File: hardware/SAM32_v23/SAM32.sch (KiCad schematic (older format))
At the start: 54 parts, among them J1 10118194-0001LF, J2 Conn_01x14, J3 5031821852, J4 B2B-PH-SM4-TB, J5 NPTC072KFMS-RC, J7 Conn_01x17, J96 MOUNTINGHOLE2.5, J97 MOUNTINGHOLE2.5, Q3 DMG341, SW1 KMR231NG LFS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

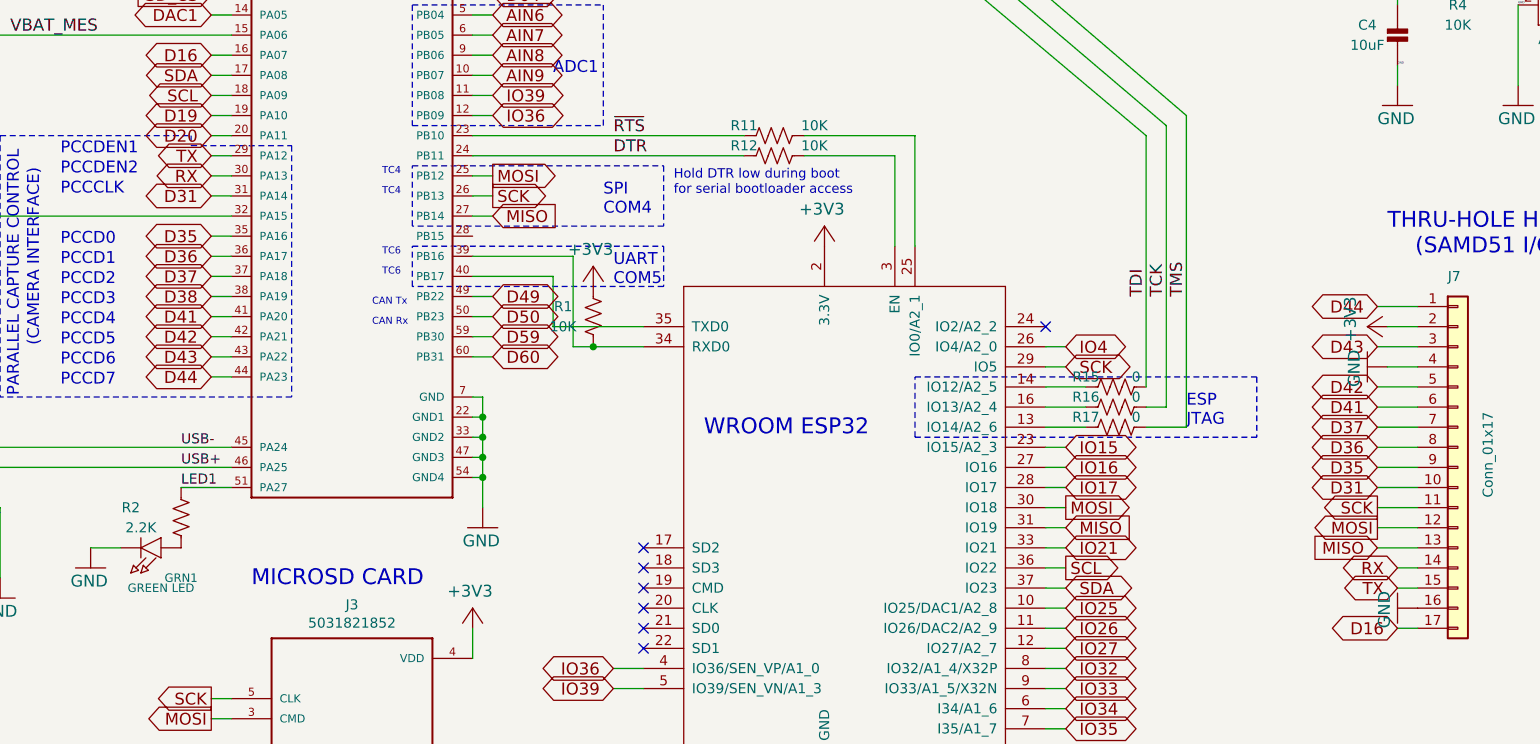
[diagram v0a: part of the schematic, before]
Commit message: adding esp32SPI firmware and clarification edits on v23 schematic
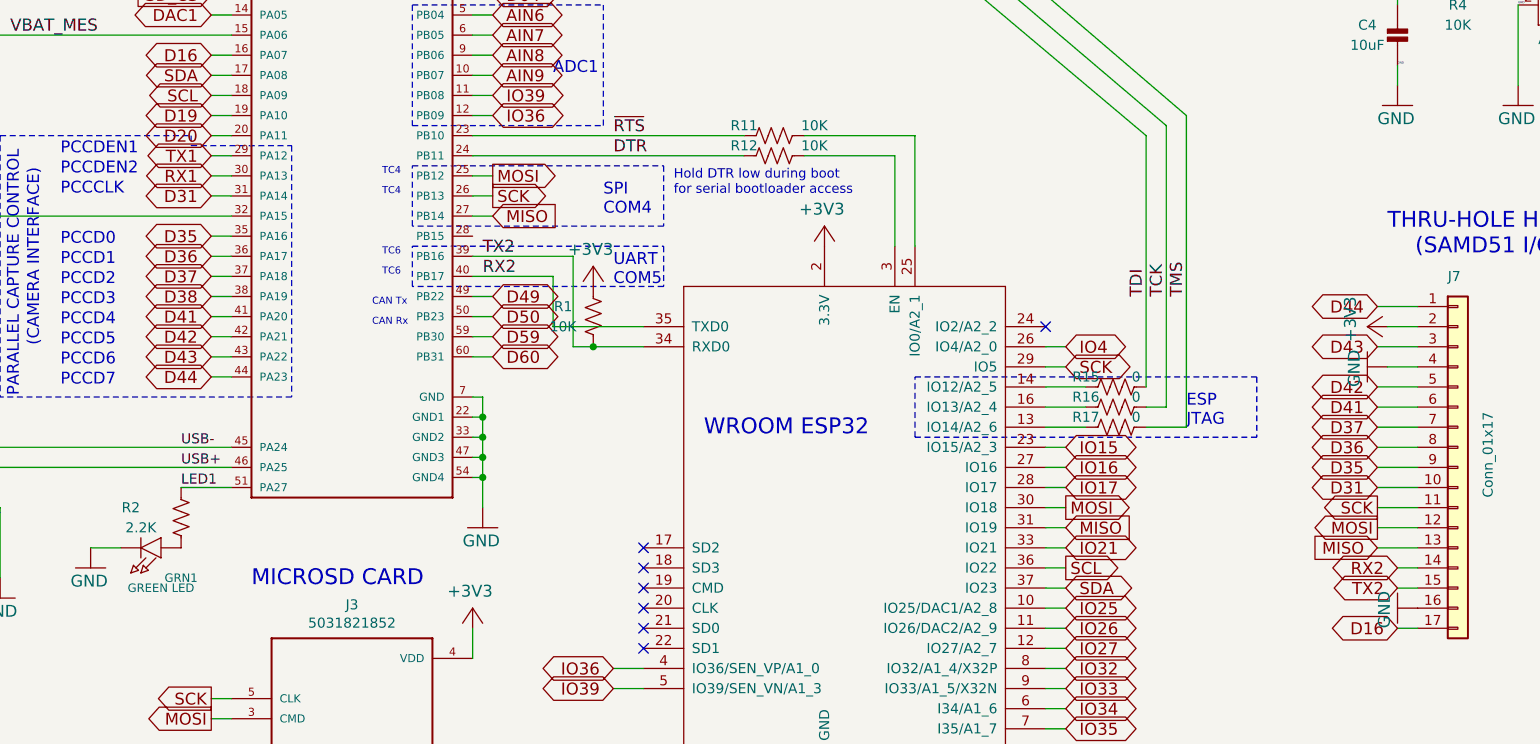
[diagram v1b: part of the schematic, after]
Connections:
- net TX2: now reaches R1.2, U2.39 (PB16), U3.34 (RXD0)
- net TX2: now also J7.15 (Pin_15)
- net RX2: now reaches U2.40 (PB17), U3.35 (TXD0)
- net RX2: now also J7.14 (Pin_14)
- net RX renamed RX1
- net RX1: no longer J7.14 (Pin_14)
- net TX renamed TX1
- net TX1: no longer J7.15 (Pin_15)
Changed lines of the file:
@@
 EESchema Schematic File Version 4
-LIBS:SAM32-cache
 EELAYER 29 0
 EELAYER END
@@
 D20
 Text GLabel 3000 3600 0    60   BiDi ~ 0
-RX
+RX1
 Text GLabel 3000 3500 0    60   BiDi ~ 0
-TX
+TX1
 Text GLabel 3000 3700 0    60   BiDi ~ 0
 D31
@@
 	9000 5550 8900 5550
 Text GLabel 8900 5550 0    60   BiDi ~ 0
-RX
+RX2
 Text GLabel 8900 5650 0    60   BiDi ~ 0
-TX
+TX2
 Wire Wire Line
 	9000 5150 8800 5150
@@
 Text GLabel 10200 4250 2    60   BiDi ~ 0
 D38
+Text Label 4350 4000 0    60   ~ 0
+TX2
+Text Label 4350 4100 0    60   ~ 0
+RX2
 $EndSCHEMATC

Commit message: making v23 easier to clone and work on locally
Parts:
- Q3: footprint Adafruit Feather M4 Express:SOT23-R -> Package_TO_SOT_SMD:SOT-23
- U4, U5: footprint Adafruit Feather M4 Express:SOT23-5 -> Package_TO_SOT_SMD:SOT-23-5
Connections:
- net DTR: now also R11.1, U2.23 (PB10); no longer R12.1, U2.24 (PB11)
- net ~RTS: now also R12.1, U2.24 (PB11); no longer R11.1, U2.23 (PB10)
- net RX1 renamed RX
- net RX: now also J7.14 (Pin_14)
- net RX2: no longer names the net of U2.40 (PB17), U3.35 (TXD0)
- net RX2: no longer J7.14 (Pin_14)
- net TX1 renamed TX
- net TX: now also J7.15 (Pin_15)
- net TX2: no longer names the net of R1.2, U2.39 (PB16), U3.34 (RXD0)
- net TX2: no longer J7.15 (Pin_15)
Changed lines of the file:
@@
 EESchema Schematic File Version 4
+LIBS:SAM32-cache
 EELAYER 29 0
 EELAYER END
@@
 F 0 "U5" H 9600 2890 42  0000 L BNN
 F 1 "AP2112K-3.3TRG1" H 9600 2350 42  0000 L BNN
-F 2 "Adafruit Feather M4 Express:SOT23-5" H 9900 2650 50  0001 C CNN
+F 2 "Package_TO_SOT_SMD:SOT-23-5" H 9900 2650 50  0001 C CNN
 F 3 "" H 9900 2650 50  0001 C CNN
 	1    9900 2650
@@
 F 0 "Q3" H 9200 2200 42  0000 L BNN
 F 1 "DMG341" H 9150 2050 42  0000 L BNN
-F 2 "Adafruit Feather M4 Express:SOT23-R" H 9450 2250 50  0001 C CNN
+F 2 "Package_TO_SOT_SMD:SOT-23" H 9450 2250 50  0001 C CNN
 F 3 "" H 9450 2250 50  0001 C CNN
 	1    9450 2250
@@
 F 0 "U4" H 8700 1400 42  0000 L BNN
 F 1 "MCP73831T-2ACI/OT" H 8400 900 42  0000 L BNN
-F 2 "Adafruit Feather M4 Express:SOT23-5" H 8750 1400 50  0001 C CNN
+F 2 "Package_TO_SOT_SMD:SOT-23-5" H 8750 1400 50  0001 C CNN
 F 3 "" H 8750 1400 50  0001 C CNN
 	1    8750 1400
@@
 	1650 4750 1650 4850
 Text Label 5000 3400 0    59   ~ 0
+DTR
+Text Label 5000 3500 0    59   ~ 0
 ~RTS
-Text Label 5000 3500 0    59   ~ 0
-DTR
 Text Label 2850 5050 0    50   ~ 0
 USB+
@@
 D20
 Text GLabel 3000 3600 0    60   BiDi ~ 0
-RX1
+RX
 Text GLabel 3000 3500 0    60   BiDi ~ 0
-TX1
+TX
 Text GLabel 3000 3700 0    60   BiDi ~ 0
 D31
@@
 	9000 5550 8900 5550
 Text GLabel 8900 5550 0    60   BiDi ~ 0
-RX2
+RX
 Text GLabel 8900 5650 0    60   BiDi ~ 0
-TX2
+TX
 Wire Wire Line
 	9000 5150 8800 5150
@@
 Text GLabel 10200 4250 2    60   BiDi ~ 0
 D38
-Text Label 4350 4000 0    60   ~ 0
-TX2
-Text Label 4350 4100 0    60   ~ 0
-RX2
 $EndSCHEMATC
